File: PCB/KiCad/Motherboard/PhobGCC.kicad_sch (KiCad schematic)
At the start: 66 parts, among them J1 Conn_01x06_Female, J2 Conn_01x04_Female, J3 Conn_01x01_Male, J5 Conn_01x02_Male, Q1 Q_NMOS_GSD, Q2 Q_PMOS_GDS, Q3 Q_NMOS_GSD, SW1 A, SW10 Dup, SW11 Dright, SW12 Ddown, SW2 B, SW3 X, SW4 Y, SW5 Start, SW6 L, SW7 R, SW9 Dleft, U1 Teensy4.0, U2 2x DRV5053CAQLPGM Hall Effect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, U3 GP2S60-MFG, U4 GP2S60-MFG

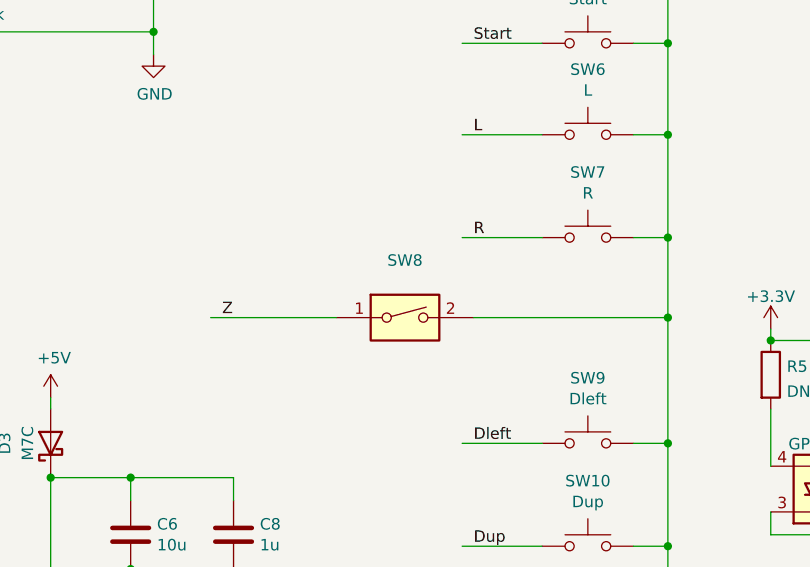
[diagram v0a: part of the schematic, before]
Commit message: Consolidated footprints to PhobGCC library
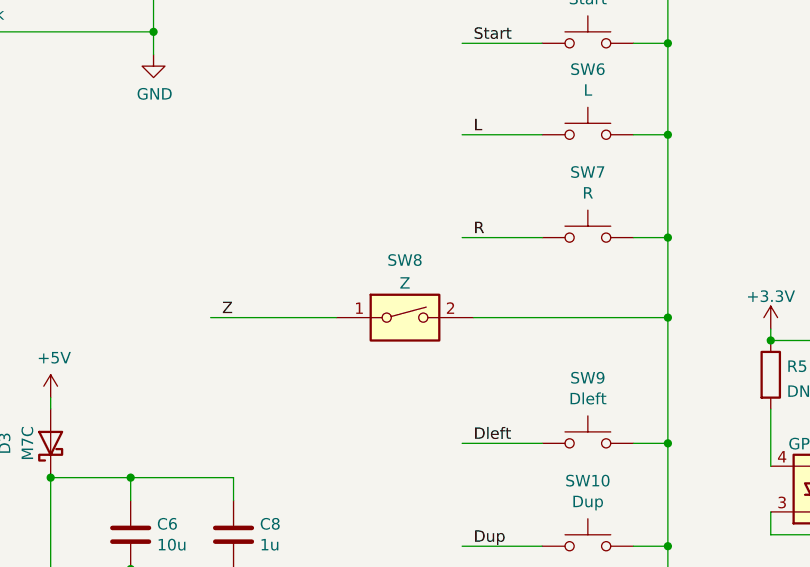
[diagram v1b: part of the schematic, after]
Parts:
- C1, C2, C3, C4, C5, C6, C7: footprint Capacitors_SMD:C_0603_HandSoldering -> (none)
- C10, C11, C12, C13, C8, C9: footprint Capacitor_SMD:C_0603_1608Metric_Pad1.08x0.95mm_HandSolder -> (none)
- D2, D3: footprint Diode_SMD:D_SOD-123 -> (none)
- F1: footprint Resistor_SMD:R_1206_3216Metric -> (none)
- J2: footprint Pin_Headers:Pin_Header_Straight_1x04_Pitch2.00mm -> (none)
- J3: footprint Connector_PinHeader_2.54mm:PinHeader_1x01_P2.54mm_Vertical -> (none)
- Q1, Q2, Q3: footprint Package_TO_SOT_SMD:SOT-23 -> (none)
- R1, R10, R11, R12, R13, R14, R15, R2, R3, R4, R5, R6, R7, R8, R9: footprint Resistor_SMD:R_0603_1608Metric_Pad0.98x0.95mm_HandSolder -> (none)
- SW8: value (none) -> Z

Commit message: 1.2.3 changes
omron tactile z support, larger c stick pin holes, relocated C10 from underneath button pad
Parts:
- C1, C2, C3, C4, C5, C6, C7: footprint (none) -> PhobGCC_Footprints:C_0603_HandSoldering
- C10, C11, C12, C13, C8, C9: footprint (none) -> PhobGCC_Footprints:C_0603_1608Metric_Pad1.08x0.95mm_HandSolder
- D2, D3: footprint (none) -> PhobGCC_Footprints:D_SOD-123
- F1: footprint (none) -> PhobGCC_Footprints:Fuse_1206_3216Metric
- J2: footprint (none) -> PhobGCC_Footprints:PinHeader_1x04_P2.00mm_Vertical
- J3: footprint (none) -> PhobGCC_Footprints:PinHeader_1x01_P2.54mm_Vertical
- Q1, Q2, Q3: footprint (none) -> PhobGCC_Footprints:SOT-23
- R1, R11, R12, R13, R14, R15, R2, R3, R4: footprint (none) -> PhobGCC_Footprints:R_0603_1608Metric_Pad0.98x0.95mm_HandSolder
- R10, R5, R6, R7, R8, R9: footprint (none) -> PhobGCC_Footprints:R_0603_1608_DNP
- SW8: footprint PhobGCC_Footprints:Z_Switch_Edge -> (none)
